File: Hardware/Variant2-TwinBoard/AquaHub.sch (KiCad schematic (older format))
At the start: 65 parts, among them J1 Screw_Terminal_01x02, J10 PinHeader6, J13 PinHeader2, J14 PinHeader3, J2 Screw_Terminal_01x02, J3 Screw_Terminal_01x02, J4 Screw_Terminal_01x02, J5 Screw_Terminal_01x02, J6 Screw_Terminal_01x02, J8 Screw_Terminal_01x02, J9 PinHeader3, K1 5A Relay, K2 5A Relay, K3 5A Relay, K4 5A Relay, K5 5A Relay, K6 5A Relay, Q1 BSS138, Q2 2SC1815, U1 ESP32-WROOM, U2 Current Sense, U3 1A 3.3V, U4 Low-Side Driver, U5 1A 5V, U7 DS1307+, Y1 32.768KHz

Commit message: New TwinBoard layout
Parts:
- removed J9: PinHeader3, Connector_PinHeader_2.54mm:PinHeader_1x03_P2.54mm_Vertical, symbol AquaHub-rescue:Conn_01x03-Connector_Generic
- removed Q1: BSS138, Package_TO_SOT_SMD:SOT-23, symbol AquaHub-rescue:BSS138-Transistor_FET
- removed R2: 2.2K, Resistor_SMD:R_0603_1608Metric_Pad1.05x0.95mm_HandSolder, symbol AquaHub-rescue:R-Device
- removed R3: 3.3K, Resistor_SMD:R_0603_1608Metric_Pad1.05x0.95mm_HandSolder, symbol AquaHub-rescue:R-Device
- removed R8, R9: 10k, Resistor_SMD:R_0603_1608Metric_Pad1.05x0.95mm_HandSolder, symbol AquaHub-rescue:R-Device
- added H11, H12, H13, H14, H15, H16, H17, H18: MountingHole, AquaFootprints:Breakaway 1mm, symbol Mechanical:MountingHole
- added TP5: Test_12V_GND, TestPoint:TestPoint_Keystone_5010-5014_Multipurpose, symbol AquaHub-rescue:TestPoint-Connector
- added TP6: TEST_5V_GND, TestPoint:TestPoint_Keystone_5010-5014_Multipurpose, symbol AquaHub-rescue:TestPoint-Connector
- BT1, C1, C2, C3, C4, C5, C6, C7, C8, F1, J1, J2, J3, J4, J5, J6, J8, K1, K2, K3, K4, K5, K6, Q2, R1, R10, R11, R5, R6, RV1, U1, U2, U3, U4, U5, Y1: Vendor (none) -> Mouser
- H1, H10, H2, H3, H4, H5, H6, H7, H8, H9: Vendor (none) -> n/a
- LS1: symbol AquaHub-rescue:Speaker_Crystal-Device -> Device:Speaker_Crystal; Vendor (none) -> Mouser
- R12, R13, R4: value 4.7K -> 4.7k; Vendor (none) -> Mouser
- TP1: value TestPoint -> TEST_5V; Vendor (none) -> n/a
- TP2: value TestPoint -> Test_3V3; Vendor (none) -> n/a
- TP3: value TestPoint -> Test_3V3_GND; Vendor (none) -> n/a
- TP4: value TestPoint -> Test_12V; Vendor (none) -> n/a
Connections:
- net +3V3: no longer BT1.1 (+), U7.3 (VBAT)
- net GND: now also TP5.1, TP6.1
- net Panel_INT: no longer U1.31 (IO19)
- net Flow_Sense: no longer names the net of U1.27 (IO16)
- net Panel_LED_33: no longer names the net of U1.16 (IO13)
- net Panel_SCL renamed SCL
- net Panel_SDA renamed SDA
- new net +BATT: BT1.1 (+), U7.3 (VBAT)
- no-connect marks 18 -> 21
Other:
- note added: "I2C Address: 0x68 1101000"
- note added: "Mounting Holes"
- note removed: "Flow Sensor"
- note removed: "Logic-Level Shifter"
- note removed: "Simple voltage\ndivider to get the\n5V signal to 3.3V."
- note removed: "This is a simple logic level shifter to drive \nthe 5V NeoPixels from the 3.3V signal."
- moved on the sheet: BT1, C2, F1, H1, H10, H2, H3, H4, H5, H6, H7, H8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

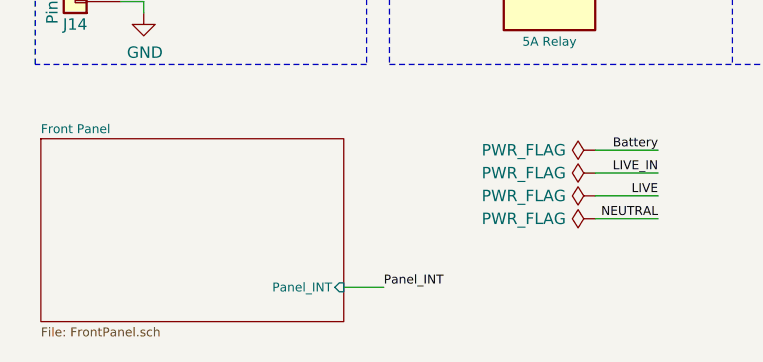
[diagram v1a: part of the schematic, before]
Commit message: Removed old variants
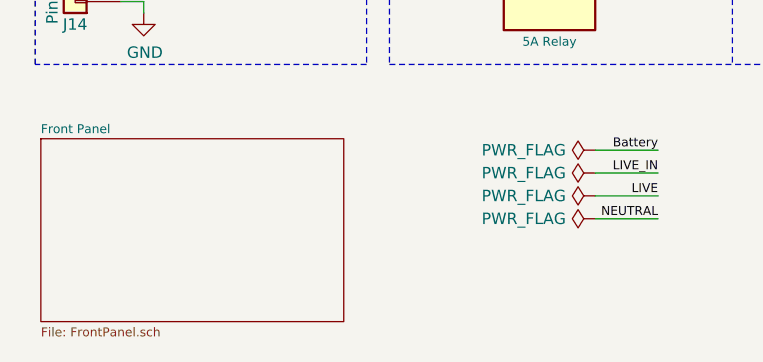
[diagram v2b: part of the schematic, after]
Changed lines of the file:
@@
 F0 "Front Panel" 39
 F1 "FrontPanel.sch" 39
-F2 "Panel_INT" I R 1950 7450 39
 $EndSheet
 Wire Wire Line
@@
 Wire Wire Line
 	9500 4525 9500 4775
-Wire Wire Line
-	1950 7450 2125 7450
-Text Label 2125 7450 0    39   ~ 0
-Panel_INT
 Text Label 6150 4725 0    39   ~ 0
 POW1
